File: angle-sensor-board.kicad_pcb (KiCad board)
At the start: 2 copper layers, 13 x 11 mm, 10 parts, among them J1 Picoblade 5 pin, U1 AS5055A

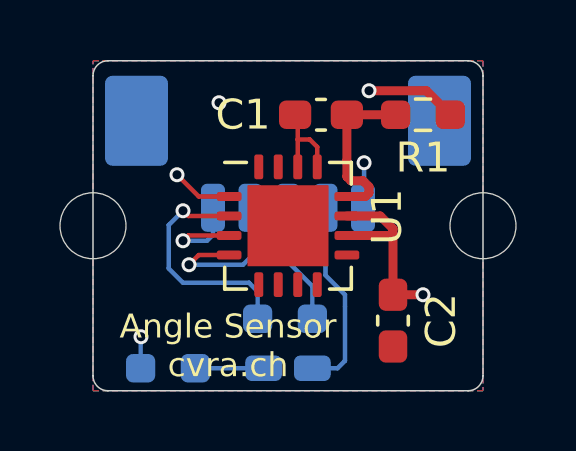
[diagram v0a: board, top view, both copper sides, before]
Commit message: Add some solder jumpers to select modes
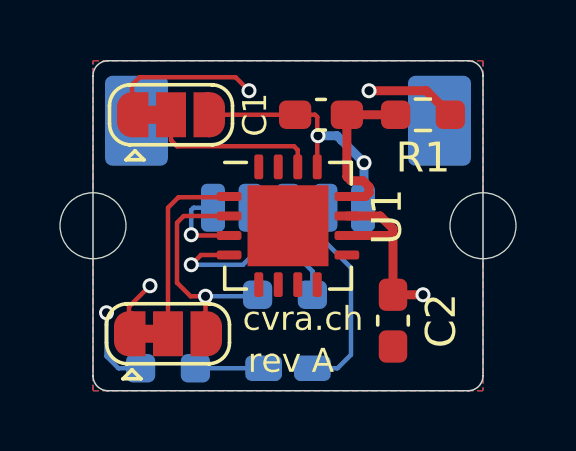
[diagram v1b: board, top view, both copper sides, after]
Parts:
- added JP1: SolderJumper_3_Bridged12, Jumper:SolderJumper-3_P1.3mm_Bridged12_RoundedPad1.0x1.5mm, F.Cu at (32.6, 31.8)
- added JP2: SolderJumper_3_Bridged12, Jumper:SolderJumper-3_P1.3mm_Bridged12_RoundedPad1.0x1.5mm, F.Cu at (32.5, 39.1)
- moved R3 0.80 mm to (36.4, 37.8)
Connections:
- U1 pad 1: +3V3 -> Net-(JP2-Pad2)
- U1 pad 14: GND -> Net-(JP1-Pad2)
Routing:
- net Net-(JP2-Pad2): track 0.00 -> 6.89 mm
- net GND: track 5.76 -> 11.6 mm
- net Net-(JP1-Pad2): track 0.00 -> 5.77 mm
- net +3V3: track 18.1 -> 23.8 mm, vias 3 -> 4
- net Net-(J1-Pad3): track 4.04 -> 3.24 mm
- net /MISO: track 7.92 -> 8.50 mm
- net /SCK: track 3.59 -> 3.03 mm
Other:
- board text added: "angle sensor"
- board text added: "cvra.ch"
- board text added: "rev A"
- board text removed: "Angle Sensor cvra.ch"
